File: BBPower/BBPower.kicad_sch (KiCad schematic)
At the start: 2 parts, among them J1 USB_C_Receptacle, U1 CYPD3177-24LQ

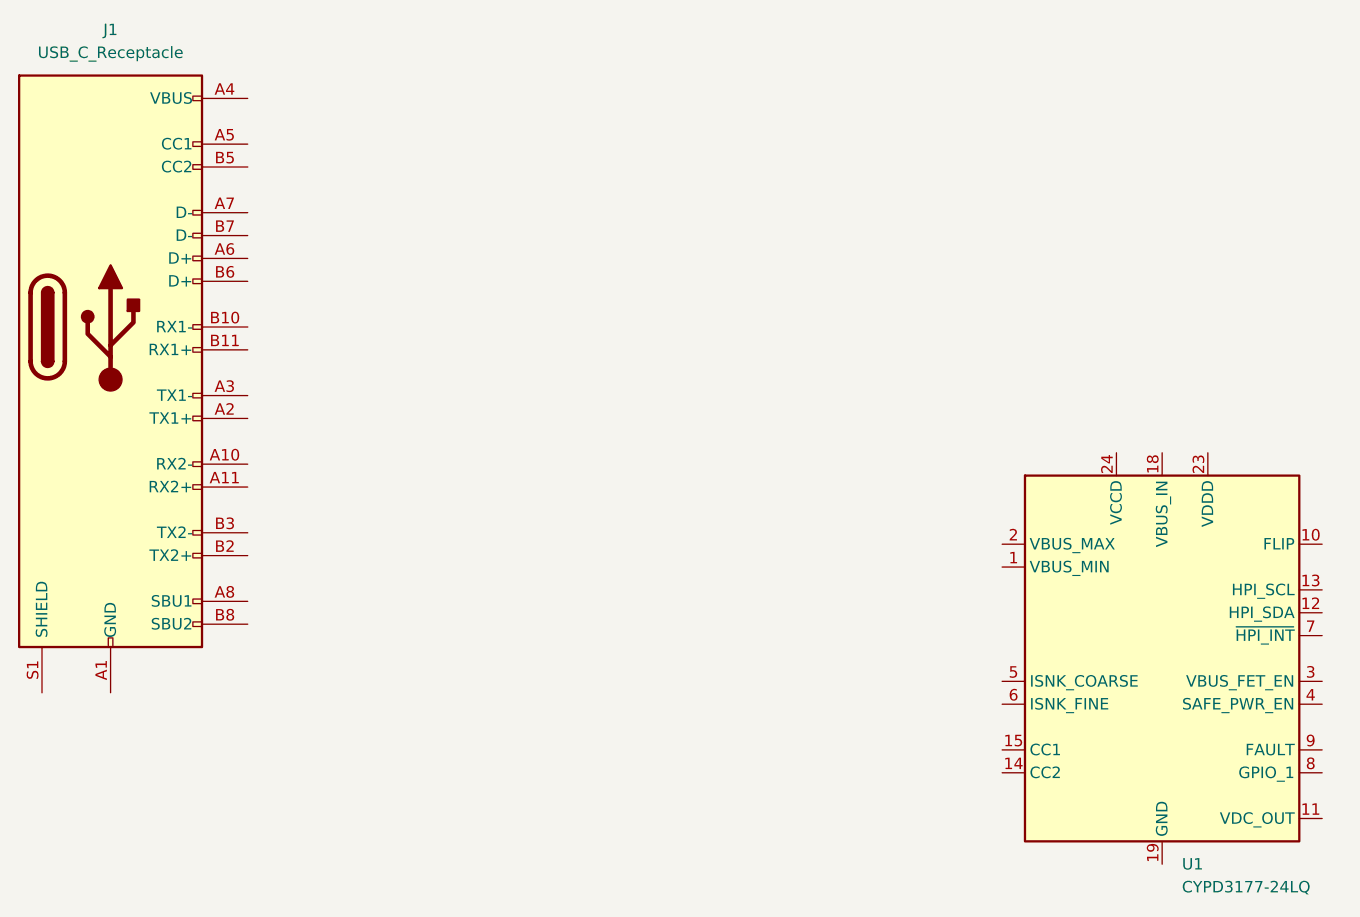
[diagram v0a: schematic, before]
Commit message: changed chip to decoy module
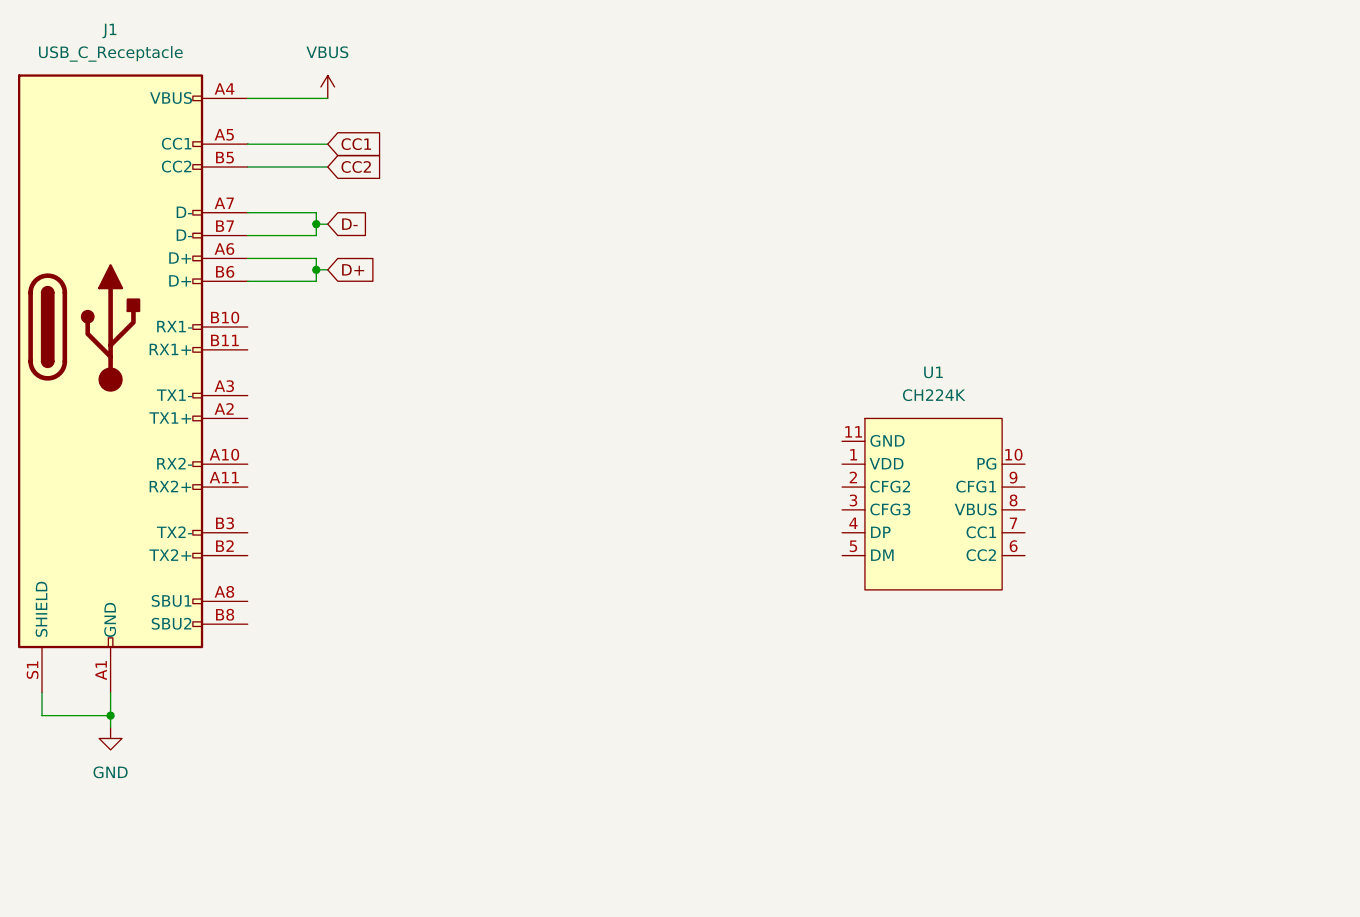
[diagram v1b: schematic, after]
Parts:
- removed U1: CYPD3177-24LQ, Package_DFN_QFN:QFN-24-1EP_4x4mm_P0.5mm_EP2.75x2.75mm, symbol Interface_USB:CYPD3177-24LQ
- added U1: CH224K, tyk_common:ESSOP-10, symbol wch_mcu_peripheral:CH224K
- J1: footprint (none) -> Connector_USB:USB_C_Receptacle_Molex_105450-0101
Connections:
- net GND: now reaches J1.A1 (GND), J1.A12 (GND), J1.B1 (GND), J1.B12 (GND)
- net GND: now also J1.S1 (SHIELD)
- net VBUS: now reaches J1.A4 (VBUS), J1.A9 (VBUS), J1.B4 (VBUS), J1.B9 (VBUS)
- net CC1: now reaches J1.A5 (CC1)
- net D+: now reaches J1.A6 (D+)
- net D+: now also J1.B6 (D+)
- net D-: now reaches J1.A7 (D-)
- net D-: now also J1.B7 (D-)
- net CC2: now reaches J1.B5 (CC2)

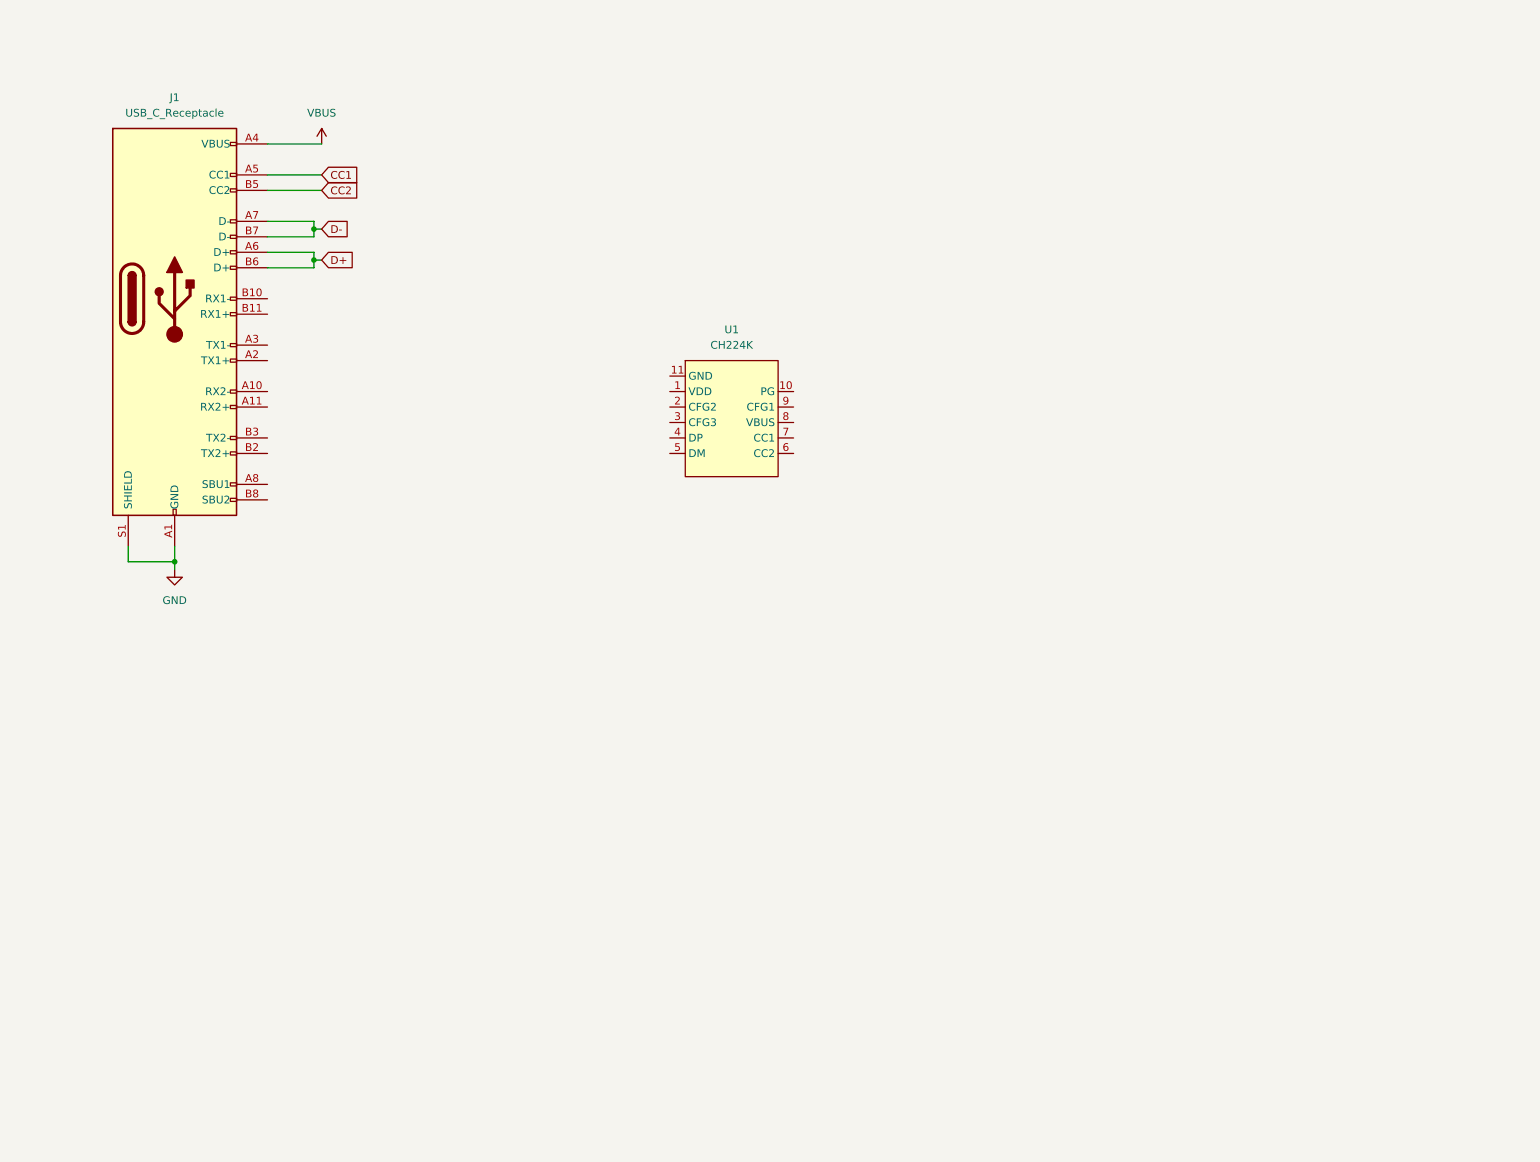
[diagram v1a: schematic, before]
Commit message: schematic layout
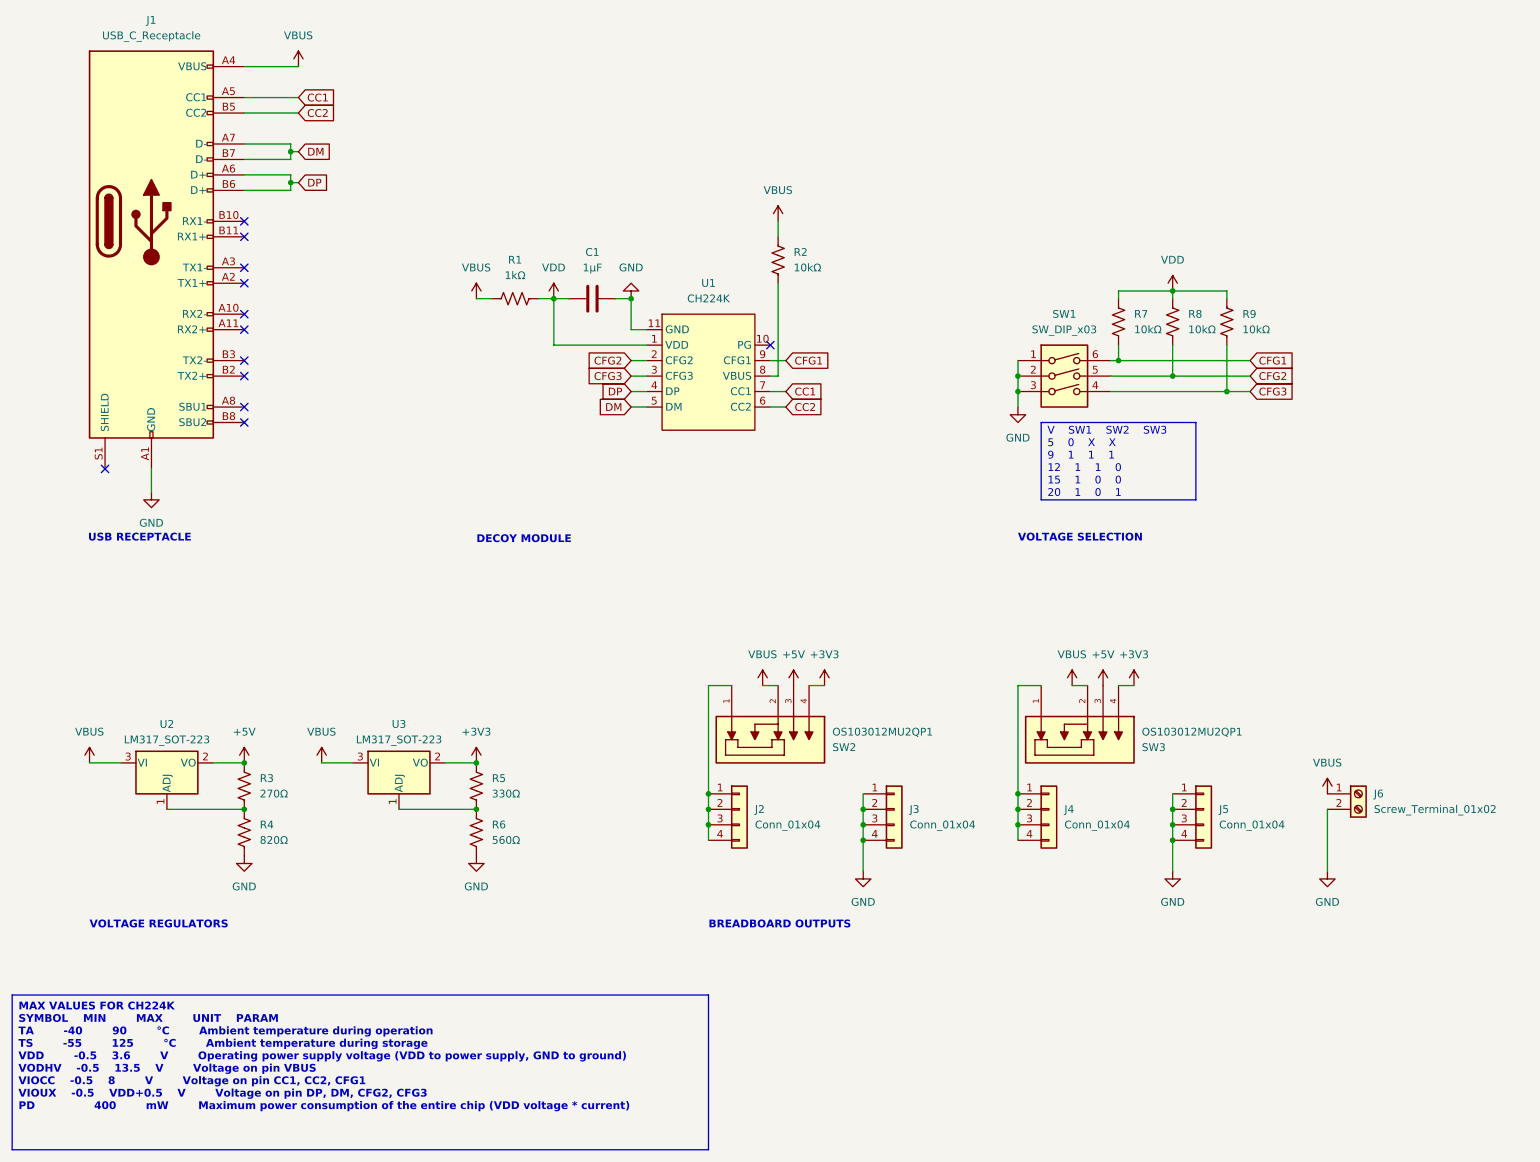
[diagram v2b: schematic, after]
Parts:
- added C1: 1μF, Capacitor_SMD:C_1206_3216Metric_Pad1.33x1.80mm_HandSolder, symbol Device:C
- added J2, J3, J4, J5: Conn_01x04, Connector_PinHeader_2.54mm:PinHeader_1x04_P2.54mm_Vertical, symbol Connector_Generic:Conn_01x04
- added J6: Screw_Terminal_01x02, TerminalBlock_TE-Connectivity:TerminalBlock_TE_282834-2_1x02_P2.54mm_Horizontal, symbol Connector:Screw_Terminal_01x02
- added R1: 1kΩ, Resistor_SMD:R_1206_3216Metric_Pad1.30x1.75mm_HandSolder, symbol Device:R_US
- added R2, R7, R8, R9: 10kΩ, Resistor_SMD:R_1206_3216Metric_Pad1.30x1.75mm_HandSolder, symbol Device:R_US
- added R3: 270Ω, Resistor_SMD:R_1206_3216Metric_Pad1.30x1.75mm_HandSolder, symbol Device:R_US
- added R4: 820Ω, Resistor_SMD:R_1206_3216Metric_Pad1.30x1.75mm_HandSolder, symbol Device:R_US
- added R5: 330Ω, Resistor_SMD:R_1206_3216Metric_Pad1.30x1.75mm_HandSolder, symbol Device:R_US
- added R6: 560Ω, Resistor_SMD:R_1206_3216Metric_Pad1.30x1.75mm_HandSolder, symbol Device:R_US
- added SW1: SW_DIP_x03, Button_Switch_SMD:SW_DIP_SPSTx03_Slide_9.78x9.8mm_W8.61mm_P2.54mm, symbol Switch:SW_DIP_x03
- added SW2, SW3: OS103012MU2QP1, Library:SW_OS103012MU2QP1, symbol New_Library:OS103012MU2QP1
- added U2, U3: LM317_SOT-223, Package_TO_SOT_SMD:SOT-223-3_TabPin2, symbol Regulator_Linear:LM317_SOT-223
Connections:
- net D+ is gone; now on net DP: J1.A6 (D+), J1.B6 (D+)
- net D- is gone; now on net DM: J1.A7 (D-), J1.B7 (D-)
- net CC1: now also U1.7 (CC1)
- net CC2: now also U1.6 (CC2)
- net GND: now also U1.11 (GND), C1.2, J3.1 (Pin_1), J3.2 (Pin_2), J3.3 (Pin_3), J3.4 (Pin_4), J5.1 (Pin_1), J5.2 (Pin_2), J5.3 (Pin_3), J5.4 (Pin_4), J6.2 (Pin_2), R4.2, R6.2, SW1.1, SW1.2, SW1.3; no longer J1.S1 (SHIELD)
- net VBUS: now also J6.1 (Pin_1), R1.1, R2.2, SW2.2, SW3.2, U2.3 (VI), U3.3 (VI)
- net VDD: now reaches U1.1 (VDD)
- net VDD: now also C1.1, R1.2, R7.2, R8.2, R9.2
- net CFG2: now reaches U1.2 (CFG2)
- net CFG2: now also R8.1, SW1.5
- net CFG3: now reaches U1.3 (CFG3)
- net CFG3: now also R9.1, SW1.4
- net DP: now reaches U1.4 (DP)
- net DM: now reaches U1.5 (DM)
- net at U1.8 (VBUS): now also R2.1
- net CFG1: now reaches U1.9 (CFG1)
- net CFG1: now also R7.1, SW1.6
- new net: R3.2, R4.1, U2.1 (ADJ)
- new net: R5.2, R6.1, U3.1 (ADJ)
- new net: J4.1 (Pin_1), J4.2 (Pin_2), J4.3 (Pin_3), J4.4 (Pin_4), SW3.1
- new net: J2.1 (Pin_1), J2.2 (Pin_2), J2.3 (Pin_3), J2.4 (Pin_4), SW2.1
- new net +3V3: R5.1, SW2.4, SW3.4, U3.2 (VO)
- new net +5V: R3.1, SW2.3, SW3.3, U2.2 (VO)
- no-connect marks 0 -> 12
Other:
- note added: "BREADBOARD OUTPUTS"
- note added: "DECOY MODULE"
- note added: "USB RECEPTACLE"
- note added: "VOLTAGE REGULATORS"
- note added: "VOLTAGE SELECTION"
- title: (none) -> USB-C PD POWER SUPPLY BREADBOARD
- moved on the sheet: J1, U1

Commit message: started pcb layout
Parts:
- U1: footprint tyk_common:ESSOP-10 -> Package_SO:SSOP-10-1EP_3.9x4.9mm_P1mm_EP2.1x3.3mm
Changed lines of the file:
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@@
 		)
 	)
-	(text_box "MAX VALUES FOR CH224K\nSYMBOL	MIN		MAX		UNIT	PARAM\nTA		-40		90		°C		Ambient temperature during operation\nTS		-55		125		°C		Ambient temperature during storage\nVDD		-0.5	3.6		V		Operating power supply voltage (VDD to power supply, GND to ground) \nVODHV	-0.5	13.5	V		Voltage on pin VBUS\nVIOCC	-0.5	8		V		Voltage on pin CC1, CC2, CFG1 \nVIOUX	-0.5	VDD+0.5	V		Voltage on pin DP, DM, CFG2, CFG3 \nPD				400		mW		Maximum power consumption of the entire chip (VDD voltage * current)\n"
+	(text_box "MAX VALUES FOR CH224K\n\nSYMBOL	MIN		MAX		UNIT	PARAM\nTA		-40		90		°C		Ambient temperature during operation\nTS		-55		125		°C		Ambient temperature during storage\nVDD		-0.5	3.6		V		Operating power supply voltage (VDD to power supply, GND to ground) \nVODHV	-0.5	13.5	V		Voltage on pin VBUS\nVIOCC	-0.5	8		V		Voltage on pin CC1, CC2, CFG1 \nVIOUX	-0.5	VDD+0.5	V		Voltage on pin DP, DM, CFG2, CFG3 \nPD				400		mW		Maximum power consumption of the entire chip (VDD voltage * current)\n"
 		(exclude_from_sim no)
 		(at 12.7 177.8 0)
@@
 			(font
 				(size 1.27 1.27)
-				(bold yes)
 			)
 			(justify left top)
 		)
 	)
-	(text_box "V	SW1	SW2	SW3\n5	0	X	X\n9	1	1	1\n12	1	1	0\n15	1	0	0\n20	1	0	1"
-		(exclude_from_sim no)
-		(at 181.61 83.82 0)
-		(size 25.4 12.7)
+	(text_box "DIP VOLTAGE SELECTION\n\nV	SW1	SW2	SW3\n5	0	X	X\n9	1	1	1\n12	1	1	0\n15	1	0	0\n20	1	0	1"
+		(exclude_from_sim no)
+		(at 128.27 177.8 0)
+		(size 25.4 25.4)
 		(stroke
 			(width 0)
@@
 				(size 1.27 1.27)
 			)
-			(justify left)
+			(justify left top)
 		)
 	)
@@
 			)
 		)
-		(property "Footprint" "tyk_common:ESSOP-10"
+		(property "Footprint" "Package_SO:SSOP-10-1EP_3.9x4.9mm_P1mm_EP2.1x3.3mm"
 			(at 129.54 90.17 0)
 			(effects

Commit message: psb layout
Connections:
- net DM: no longer J1.B7 (D-)
- net DP: no longer J1.B6 (D+)
- no-connect marks 12 -> 14
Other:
- company: (none) -> AL

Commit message: pcb updates & production file
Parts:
- J2, J3, J4, J5: now not fitted
- SW1: footprint Button_Switch_SMD:SW_DIP_SPSTx03_Slide_9.78x9.8mm_W8.61mm_P2.54mm -> Library:SW_DS04-254-1L-03BK
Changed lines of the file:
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@@
 		(in_bom yes)
 		(on_board yes)
-		(dnp no)
+		(dnp yes)
 		(fields_autoplaced yes)
 		(property "Reference" "J3"
@@
 		(in_bom yes)
 		(on_board yes)
-		(dnp no)
+		(dnp yes)
 		(fields_autoplaced yes)
 		(property "Reference" "J2"
@@
 		(in_bom yes)
 		(on_board yes)
-		(dnp no)
+		(dnp yes)
 		(fields_autoplaced yes)
 		(property "Reference" "J4"
@@
 			)
 		)
-		(property "Footprint" "Button_Switch_SMD:SW_DIP_SPSTx03_Slide_9.78x9.8mm_W8.61mm_P2.54mm"
+		(property "Footprint" "Library:SW_DS04-254-1L-03BK"
 			(at 185.42 78.74 0)
 			(effects
@@
 		(in_bom yes)
 		(on_board yes)
-		(dnp no)
+		(dnp yes)
 		(fields_autoplaced yes)
 		(property "Reference" "J5"
